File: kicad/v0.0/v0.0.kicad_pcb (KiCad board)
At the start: 2 copper layers, 71.4 x 69.6 mm, 53 parts, among them J1 USB_B_Micro, J2 9V_IN, J3 MOTOR, J4 LED, J5 BUTTON, Q1 IRF520, SW1 RST, SW2 FLASH, U1 MCP2221AxSL, U2 MAX14872ETC+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

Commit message: ready for board review/ordering
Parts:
- removed TP10, TP11, TP12, TP9: TestPoint, TestPoint:TestPoint_Pad_2.5x2.5mm
- added GPIO23: TestPoint, TestPoint:TestPoint_Pad_2.5x2.5mm, F.Cu at (173.5, 59.9)
- SW1: value RST -> RESET
- moved TP8 106.2 mm to (122.7, 64.3)
- moved TP6 0.25 mm to (166.6, 61.0)
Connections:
- TP8 pad 1: unconnected-(TP8-Pad1) -> Net-(TP8-Pad1)
- U3 pad 11: unconnected-(U3-Pad11) -> Net-(TP8-Pad1)
- U3 pad 37: unconnected-(U3-Pad37) -> Net-(U3-Pad37)
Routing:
- net Net-(U3-Pad37): track 0.00 -> 18.9 mm, vias 0 -> 2
- net Net-(TP8-Pad1): track 0.00 -> 18.0 mm, vias 0 -> 2

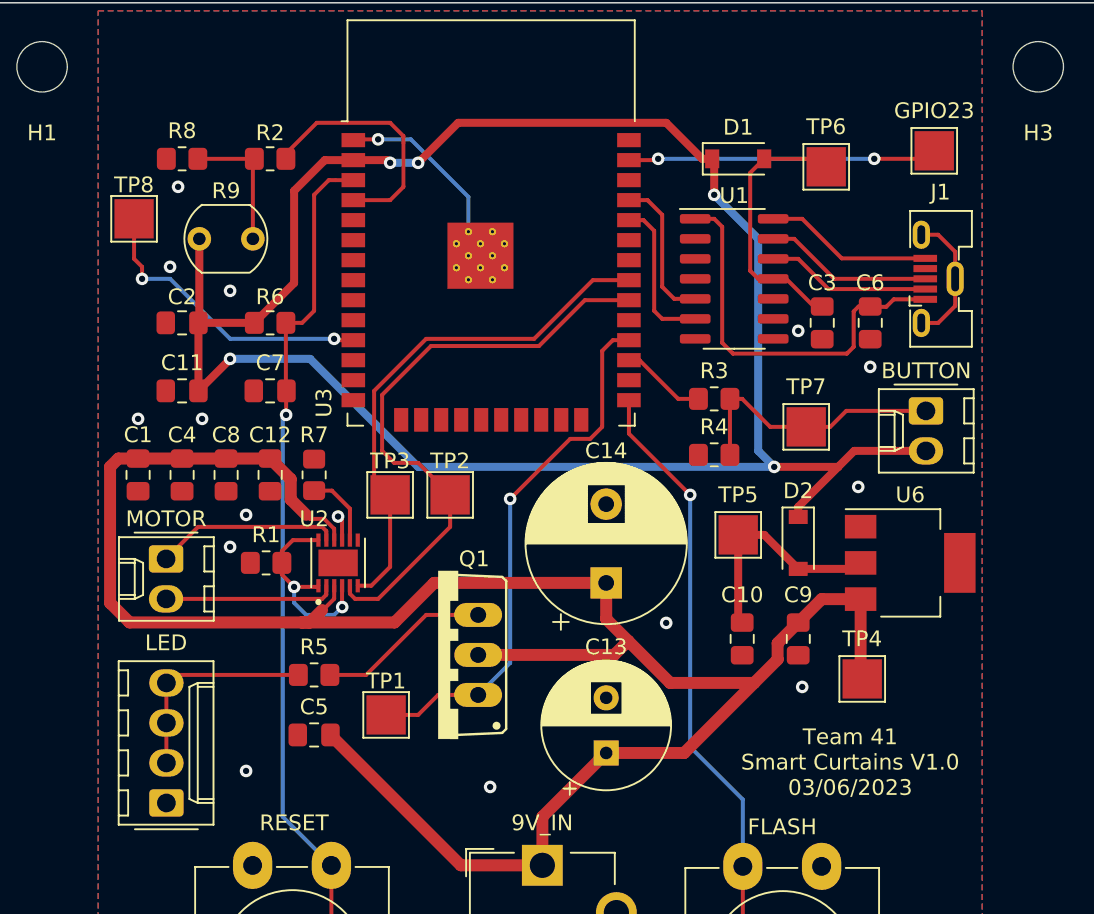
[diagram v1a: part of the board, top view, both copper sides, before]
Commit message: v0.0 has been sent to TA for printing, all future changes must be on v1.0
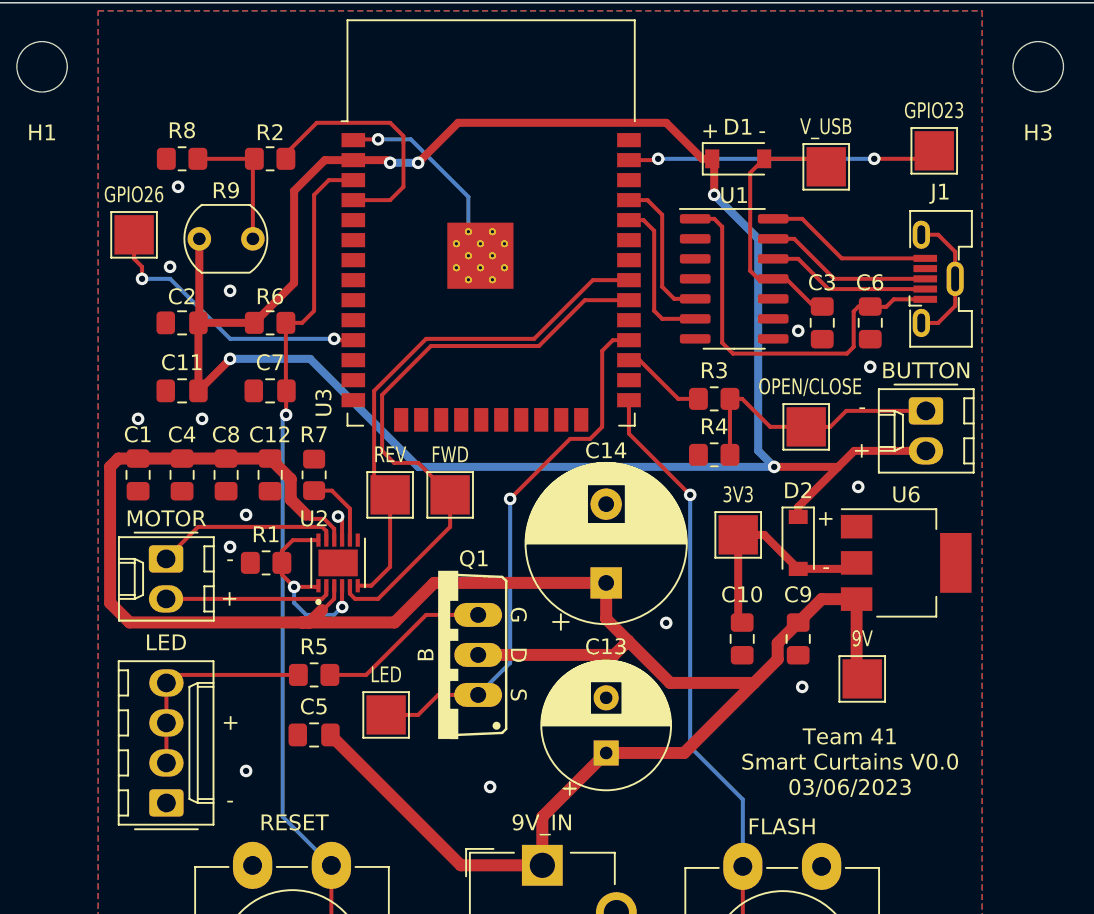
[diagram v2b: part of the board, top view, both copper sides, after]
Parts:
- removed GPIO23: TestPoint, TestPoint:TestPoint_Pad_2.5x2.5mm
- added TP9: TestPoint, TestPoint:TestPoint_Pad_2.5x2.5mm, F.Cu at (173.5, 59.9)
- moved TP8 1.02 mm to (122.7, 65.3)
- moved U6 0.25 mm to (171.7, 86.1)
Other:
- board text added: "3V3"
- board text added: "9V"
- board text added: "FWD"
- board text added: "GPIO23"
- board text added: "GPIO26"
- board text added: "LED"
- board text added: "OPEN/CLOSE"
- board text added: "REV"
- board text added: "Team 41 Smart Curtains V0.0 03/06/2023"
- board text added: "V_USB"
- board text removed: "Team 41 Smart Curtains V1.0 03/06/2023"

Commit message: v0.0 pcb checkin
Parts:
- added R10: 1k, Resistor_SMD:R_0805_2012Metric_Pad1.20x1.40mm_HandSolder, F.Cu at (159.0, 102.1)
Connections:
- U3 pad 25: Net-(SW2-Pad1) -> Net-(U3-Pad25)
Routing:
- net Net-(SW2-Pad1): track 45.1 -> 16.3 mm, vias 1 -> 0
- net Net-(U3-Pad25): track 0.00 -> 28.0 mm, vias 0 -> 2
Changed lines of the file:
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@@
   (net 59 "Net-(TP8-Pad1)")
   (net 60 "Net-(TP9-Pad1)")
+  (net 61 "Net-(U3-Pad25)")
   (footprint "Capacitor_SMD:C_0805_2012Metric_Pad1.18x1.45mm_HandSolder" (layer "F.Cu")
     (at 134.112 97.028 180)
@@
       (effects (font (size 1 1) (thickness 0.15)))
     )
-    (fp_text user "S" (at -2.54 5.08 270 unlocked) (layer "F.SilkS")
-      (effects (font (size 1 1) (thickness 0.15)))
-    )
-    (fp_text user "G" (at 2.54 5.08 270 unlocked) (layer "F.SilkS")
+    (fp_text user "S" (at 2.54 5.08 270 unlocked) (layer "F.SilkS")
+      (effects (font (size 1 1) (thickness 0.15)))
+    )
+    (fp_text user "G" (at -2.54 5.08 270 unlocked) (layer "F.SilkS")
       (effects (font (size 1 1) (thickness 0.15)))
     )
@@
       (net 46 "unconnected-(U3-Pad24)") (pinfunction "IO2") (pintype "bidirectional"))
     (pad "25" smd rect (at 8.75 8.26) (size 1.5 0.9) (layers "F.Cu" "F.Paste" "F.Mask")
-      (net 53 "Net-(SW2-Pad1)") (pinfunction "IO0") (pintype "bidirectional"))
+      (net 61 "Net-(U3-Pad25)") (pinfunction "IO0") (pintype "bidirectional"))
     (pad "26" smd rect (at 8.75 6.99) (size 1.5 0.9) (layers "F.Cu" "F.Paste" "F.Mask")
       (net 47 "unconnected-(U3-Pad26)") (pinfunction "IO4") (pintype "bidirectional"))
@@
     (pad "2" smd roundrect (at 1 0 90) (size 1.2 1.4) (layers "F.Cu" "F.Paste" "F.Mask") (roundrect_rratio 0.2083333333)
       (net 2 "GND") (pintype "passive"))
+    (model "${KICAD6_3DMODEL_DIR}/Resistor_SMD.3dshapes/R_0805_2012Metric.wrl"
+      (offset (xyz 0 0 0))
+      (scale (xyz 1 1 1))
+      (rotate (xyz 0 0 0))
+    )
+  )
+  (footprint "Resistor_SMD:R_0805_2012Metric_Pad1.20x1.40mm_HandSolder" (layer "F.Cu")
+    (at 159.004 102.108)
+    (descr "Resistor SMD 0805 (2012 Metric), square (rectangular) end terminal, IPC_7351 nominal with elongated pad for handsoldering. (Body size source: IPC-SM-782 page 72, https://www.pcb-3d.com/wordpress/wp-content/uploads/ipc-sm-782a_amendment_1_and_2.pdf), generated with kicad-footprint-generator")
+    (tags "resistor handsolder")
+    (property "Sheetfile" "v0.0.kicad_sch")
+    (property "Sheetname" "")
+    (attr smd)
+    (fp_text reference "R10" (at 0.227064 -1.778) (layer "F.SilkS")
+      (effects (font (size 1 1) (thickness 0.15)))
+    )
+    (fp_text value "1k" (at 0 1.65) (layer "F.Fab")
+      (effects (font (size 1 1) (thickness 0.15)))
+    )
+    (fp_text user "${REFERENCE}" (at 0 0) (layer "F.Fab")
+      (effects (font (size 0.5 0.5) (thickness 0.08)))
+    )
+    (fp_line (start -0.227064 0.735) (end 0.227064 0.735) (layer "F.SilkS") (width 0.12))
+    (fp_line (start -0.227064 -0.735) (end 0.227064 -0.735) (layer "F.SilkS") (width 0.12))
+    (fp_line (start -1.85 -0.95) (end 1.85 -0.95) (layer "F.CrtYd") (width 0.05))
+    (fp_line (start 1.85 0.95) (end -1.85 0.95) (layer "F.CrtYd") (width 0.05))
+    (fp_line (start 1.85 -0.95) (end 1.85 0.95) (layer "F.CrtYd") (width 0.05))
+    (fp_line (start -1.85 0.95) (end -1.85 -0.95) (layer "F.CrtYd") (width 0.05))
+    (fp_line (start 1 -0.625) (end 1 0.625) (layer "F.Fab") (width 0.1))
+    (fp_line (start -1 -0.625) (end 1 -0.625) (layer "F.Fab") (width 0.1))
+    (fp_line (start -1 0.625) (end -1 -0.625) (layer "F.Fab") (width 0.1))
+    (fp_line (start 1 0.625) (end -1 0.625) (layer "F.Fab") (width 0.1))
+    (pad "1" smd roundrect (at -1 0) (size 1.2 1.4) (layers "F.Cu" "F.Paste" "F.Mask") (roundrect_rratio 0.208333)
+      (net 61 "Net-(U3-Pad25)") (pintype "passive"))
+    (pad "2" smd roundrect (at 1 0) (size 1.2 1.4) (layers "F.Cu" "F.Paste" "F.Mask") (roundrect_rratio 0.208333)
+      (net 53 "Net-(SW2-Pad1)") (pintype "passive"))
     (model "${KICAD6_3DMODEL_DIR}/Resistor_SMD.3dshapes/R_0805_2012Metric.wrl"
       (offset (xyz 0 0 0))
@@
   (segment (start 133.604 89.408) (end 132.842 88.646) (width 0.254) (layer "B.Cu") (net 16))
   (segment (start 135.895714 88.905714) (end 135.884286 88.905714) (width 0.254) (layer "B.Cu") (net 16))
-  (segment (start 135.112 93.218) (end 137.414 93.218) (width 0.254) (layer "F.Cu") (net 17))
-  (segment (start 137.414 93.218) (end 141.224 89.408) (width 0.254) (layer "F.Cu") (net 17))
-  (segment (start 141.224 89.408) (end 144.526 89.408) (width 0.254) (layer "F.Cu") (net 17))
+  (segment (start 141.224 89.408) (end 144.526 89.408) (width 0.762) (layer "F.Cu") (net 17))
+  (segment (start 137.414 93.218) (end 141.224 89.408) (width 0.762) (layer "F.Cu") (net 17))
+  (segment (start 135.112 93.218) (end 137.414 93.218) (width 0.762) (layer "F.Cu") (net 17))
   (segment (start 126.73 60.452) (end 130.318 60.452) (width 0.25) (layer "F.Cu") (net 18))
   (segment (start 130.224 60.546) (end 130.318 60.452) (width 0.25) (layer "F.Cu") (net 18))
@@
   (segment (start 170.912 69.372) (end 170.434 69.85) (width 0.254) (layer "F.Cu") (net 48))
   (segment (start 160.702 72.818) (end 160.02 72.136) (width 0.254) (layer "F.Cu") (net 48))
-  (segment (start 154.1 77.9) (end 154.1 75.775) (width 0.254) (layer "F.Cu") (net 53))
-  (segment (start 157.988 81.788) (end 154.1 77.9) (width 0.254) (layer "F.Cu") (net 53))
+  (segment (start 161.33 105.372) (end 161.33 103.434) (width 0.254) (layer "F.Cu") (net 53))
+  (segment (start 161.33 103.434) (end 160.004 102.108) (width 0.254) (layer "F.Cu") (net 53))
   (segment (start 161.33 117.872) (end 161.33 105.372) (width 0.254) (layer "F.Cu") (net 53))
-  (via (at 157.988 81.788) (size 0.8) (drill 0.4) (layers "F.Cu" "B.Cu") (net 53))
-  (segment (start 157.988 97.79) (end 157.988 81.788) (width 0.254) (layer "B.Cu") (net 53))
-  (segment (start 157.988 97.79) (end 161.33 101.132) (width 0.254) (layer "B.Cu") (net 53))
-  (segment (start 161.33 101.132) (end 161.33 105.372) (width 0.254) (layer "B.Cu") (net 53))
   (segment (start 154.769 73.235) (end 157.226 75.692) (width 0.254) (layer "F.Cu") (net 56))
   (segment (start 154.1 73.235) (end 154.769 73.235) (width 0.254) (layer "F.Cu") (net 56))
   (segment (start 157.226 75.692) (end 158.512 75.692) (width 0.254) (layer "F.Cu") (net 56))
-  (segment (start 124.734 93.706) (end 125.222 93.218) (width 0.254) (layer "F.Cu") (net 57))
-  (segment (start 124.734 98.806) (end 124.734 96.266) (width 0.254) (layer "F.Cu") (net 57))
-  (segment (start 124.734 93.726) (end 124.734 93.706) (width 0.254) (layer "F.Cu") (net 57))
-  (segment (start 124.734 96.266) (end 124.734 93.726) (width 0.254) (layer "F.Cu") (net 57))
-  (segment (start 125.222 93.218) (end 133.112 93.218) (width 0.254) (layer "F.Cu") (net 57))
+  (segment (start 124.734 96.266) (end 124.734 93.726) (width 0.762) (layer "F.Cu") (net 57))
+  (segment (start 124.734 93.726) (end 124.734 93.706) (width 0.762) (layer "F.Cu") (net 57))
+  (segment (start 125.222 93.218) (end 133.112 93.218) (width 0.762) (layer "F.Cu") (net 57))
+  (segment (start 124.734 98.806) (end 124.734 96.266) (width 0.762) (layer "F.Cu") (net 57))
+  (segment (start 124.734 93.706) (end 125.222 93.218) (width 0.762) (layer "F.Cu") (net 57))
   (segment (start 163.068 77.47) (end 165.354 77.47) (width 0.254) (layer "F.Cu") (net 58))
   (segment (start 166.878 77.47) (end 167.894 76.454) (width 0.254) (layer "F.Cu") (net 58))
@@
   (via (at 155.956 60.452) (size 0.8) (drill 0.4) (layers "F.Cu" "B.Cu") (net 60))
   (segment (start 155.956 60.452) (end 169.672 60.452) (width 0.254) (layer "B.Cu") (net 60))
+  (segment (start 154.1 77.9) (end 154.1 75.775) (width 0.254) (layer "F.Cu") (net 61))
+  (segment (start 158.004 102.108) (end 158.004 99.33) (width 0.254) (layer "F.Cu") (net 61))
+  (segment (start 157.988 81.788) (end 154.1 77.9) (width 0.254) (layer "F.Cu") (net 61))
+  (segment (start 158.004 99.33) (end 157.988 99.314) (width 0.254) (layer "F.Cu") (net 61))
+  (via (at 157.988 81.788) (size 0.8) (drill 0.4) (layers "F.Cu" "B.Cu") (net 61))
+  (via (at 157.988 99.314) (size 0.8) (drill 0.4) (layers "F.Cu" "B.Cu") (net 61))
+  (segment (start 157.988 99.314) (end 157.988 81.788) (width 0.254) (layer "B.Cu") (net 61))
   (zone (net 2) (net_name "GND") (layers F&B.Cu) (hatch edge 0.508)
     (connect_pads (clearance 0.508))

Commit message: final versions I sent to TA, signing off for the week now
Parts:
- removed R7: 10k, Resistor_SMD:R_0805_2012Metric_Pad1.20x1.40mm_HandSolder
- added C15: 22u, Capacitor_SMD:C_0805_2012Metric_Pad1.18x1.45mm_HandSolder, F.Cu at (134.6, 89.4)
- U2: value MAX14872ETC+ -> ZXBM5210-SP; footprint MAX14872ETC_:SON50P300X300X80-13N -> Package_SO:Diodes_SO-8EP
- moved C5 11.5 mm to (145.0, 100.6)
- moved SW1 8.25 mm to (122.0, 117.8)
- moved U2 7.82 mm to (128.0, 87.9), turned to 180 degrees
- moved H1 6.37 mm to (110.5, 54.1)
- moved H2 6.37 mm to (110.5, 116.6)
- moved J3 5.87 mm to (118.9, 86.1)
- moved J4 5.85 mm to (118.9, 101.1)
- moved C1 5.84 mm to (117.1, 80.5)
- moved R1 5.61 mm to (130.6, 80.5), turned to -90 degrees
- moved C4 5.33 mm to (120.4, 80.5)
- moved C8 4.57 mm to (124.0, 80.5)
- moved C12 3.81 mm to (127.5, 80.5)
- moved J2 3.57 mm to (145.0, 105.6)
- moved SW2 2.07 mm to (163.4, 117.9)
- moved TP2 1.55 mm to (144.3, 81.5)
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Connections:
- J3 pad 1: Net-(J3-Pad1) -> Net-(U2-Pad7)
- J3 pad 2: Net-(J3-Pad2) -> Net-(U2-Pad1)
- R1 pad 1: /SNS -> +9V
- U2 pad 1: /SNS -> Net-(U2-Pad1)
- U2 pad 2: Net-(J3-Pad2) -> Net-(U2-Pad2)
- U2 pad 4: /SNS -> /FWD
- U2 pad 5: /FWD -> /REV
- U2 pad 6: /REV -> +9V
- U2 pad 7: unconnected-(U2-Pad7) -> Net-(U2-Pad7)
- U2 pad 8: Net-(R7-Pad1) -> GND
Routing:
- net +9V: track 137.7 -> 121.3 mm
- net Net-(U2-Pad1): track 0.00 -> 13.4 mm
- net /SNS: track 12.7 -> 0.00 mm, vias 2 -> 0
- net Net-(J3-Pad1): track 11.7 -> 0.00 mm
- net /REV: track 33.2 -> 44.9 mm, vias 0 -> 2
- net Net-(J3-Pad2): track 10.9 -> 0.00 mm
- net Net-(U2-Pad7): track 0.00 -> 7.67 mm
- net Net-(J4-Pad2): track 13.7 -> 19.4 mm
- net /FWD: track 38.1 -> 43.5 mm, vias 0 -> 2
- net Net-(R7-Pad1): track 4.75 -> 0.00 mm
- net Net-(U2-Pad2): track 0.00 -> 3.44 mm
- net Net-(C7-Pad1): track 60.7 -> 62.4 mm
- net Net-(R10-Pad2): track 16.3 -> 17.3 mm
- net GND: track 24.2 -> 25.1 mm, vias 16 -> 13
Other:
- board size 71.4 x 69.6 mm -> 77.2 x 69.6 mm
